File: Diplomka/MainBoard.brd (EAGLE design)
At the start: 100 x 100 mm, 44 parts, among them K1 ARK550/2, Q1 AP2012P3C-P22, Q2 BC817-40LT1SMD, Q3 SS8050-G, Q4 SS8050-G, U1 ESP32-WROOM-32, U2 AMS1117-3.3

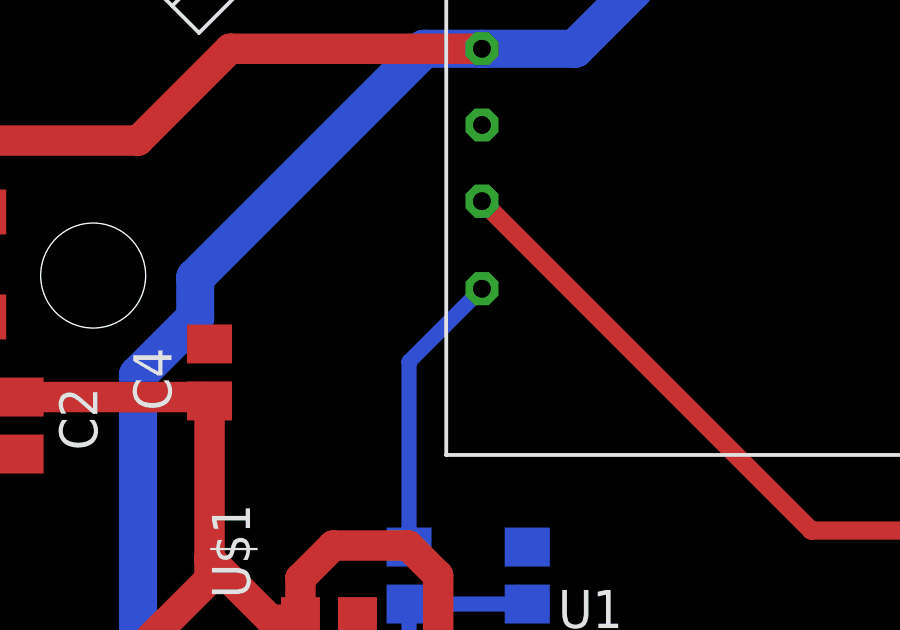
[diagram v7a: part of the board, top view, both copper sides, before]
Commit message: Opravena rozteč.
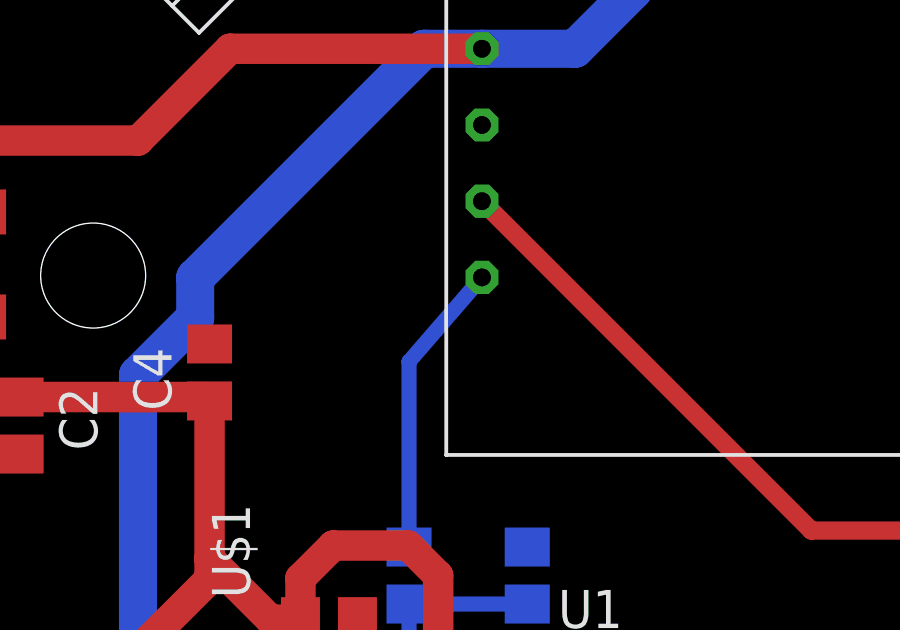
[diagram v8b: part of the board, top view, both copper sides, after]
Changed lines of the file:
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@@
 <via x="42.5" y="93.5" extent="1-16" drill="0.5" diameter="1.15" shape="octagon"/>
 <contactref element="JUM1" pad="6"/>
+<wire x1="64.97" y1="66.48" x2="85" y2="78.85" width="0" layer="19" extent="1-1"/>
+<wire x1="58.5" y1="55.26" x2="64.97" y2="66.48" width="0" layer="19" extent="1-1"/>
+<wire x1="50.835" y1="49.595" x2="58.5" y2="55.26" width="0" layer="19" extent="1-1"/>
+<wire x1="50.835" y1="48.6775" x2="50.835" y2="49.595" width="0" layer="19" extent="1-1"/>
+<wire x1="50.835" y1="47.76" x2="50.835" y2="48.6775" width="0" layer="19" extent="1-1"/>
+<wire x1="49.9175" y1="49.595" x2="50.835" y2="49.595" width="0" layer="19" extent="1-1"/>
+<wire x1="49" y1="49.595" x2="49.9175" y2="49.595" width="0" layer="19" extent="1-1"/>
+<wire x1="49" y1="48.6775" x2="49" y2="49.595" width="0" layer="19" extent="1-1"/>
+<wire x1="50.835" y1="46.8425" x2="50.835" y2="47.76" width="0" layer="19" extent="1-1"/>
+<wire x1="50.835" y1="45.925" x2="50.835" y2="46.8425" width="0" layer="19" extent="1-1"/>
+<wire x1="49" y1="47.76" x2="49" y2="48.6775" width="0" layer="19" extent="1-1"/>
+<wire x1="48.0825" y1="49.595" x2="49" y2="49.595" width="0" layer="19" extent="1-1"/>
+<wire x1="47.165" y1="49.595" x2="48.0825" y2="49.595" width="0" layer="19" extent="1-1"/>
+<wire x1="47.165" y1="48.6775" x2="47.165" y2="49.595" width="0" layer="19" extent="1-1"/>
+<wire x1="49.9175" y1="47.76" x2="50.835" y2="47.76" width="0" layer="19" extent="1-1"/>
+<wire x1="49" y1="46.8425" x2="49" y2="47.76" width="0" layer="19" extent="1-1"/>
+<wire x1="49" y1="45.925" x2="49" y2="46.8425" width="0" layer="19" extent="1-1"/>
+<wire x1="49.9175" y1="45.925" x2="50.835" y2="45.925" width="0" layer="19" extent="1-1"/>
+<wire x1="47.165" y1="47.76" x2="47.165" y2="48.6775" width="0" layer="19" extent="1-1"/>
+<wire x1="48.0825" y1="47.76" x2="49" y2="47.76" width="0" layer="19" extent="1-1"/>
+<wire x1="47.165" y1="46.8425" x2="47.165" y2="47.76" width="0" layer="19" extent="1-1"/>
+<wire x1="47.165" y1="45.925" x2="47.165" y2="46.8425" width="0" layer="19" extent="1-1"/>
+<wire x1="48.0825" y1="45.925" x2="49" y2="45.925" width="0" layer="19" extent="1-1"/>
+<wire x1="41.5" y1="55.26" x2="47.165" y2="49.595" width="0" layer="19" extent="1-1"/>
+<wire x1="44.285" y1="37.75" x2="47.165" y2="45.925" width="0" layer="19" extent="1-1"/>
+<wire x1="50.44" y1="30.68" x2="44.285" y2="37.75" width="0" layer="19" extent="1-1"/>
+<wire x1="39.47" y1="65.95" x2="41.5" y2="55.26" width="0" layer="19" extent="1-16"/>
+<wire x1="61.17" y1="33.58" x2="50.44" y2="30.68" width="0" layer="19" extent="1-1"/>
+<wire x1="35.03" y1="46.2" x2="41.5" y2="55.26" width="0" layer="19" extent="1-1"/>
+<wire x1="27" y1="43" x2="35.03" y2="46.2" width="0" layer="19" extent="1-1"/>
+<wire x1="26.495" y1="48.26" x2="27" y2="43" width="0" layer="19" extent="1-1"/>
+<wire x1="32.04" y1="37.97" x2="27" y2="43" width="0" layer="19" extent="1-1"/>
+<wire x1="29.5" y1="56.08" x2="26.495" y2="48.26" width="0" layer="19" extent="1-1"/>
+<wire x1="28.88" y1="72.72" x2="39.47" y2="65.95" width="0" layer="19" extent="1-16"/>
+<wire x1="22.6" y1="69.05" x2="28.88" y2="72.72" width="0" layer="19" extent="1-1"/>
+<wire x1="21.45" y1="73.62" x2="22.6" y2="69.05" width="0" layer="19" extent="1-1"/>
+<wire x1="21.45" y1="77.12" x2="21.45" y2="73.62" width="0" layer="19" extent="1-1"/>
+<wire x1="16.465" y1="69.34" x2="22.6" y2="69.05" width="0" layer="19" extent="1-1"/>
+<wire x1="37.96" y1="80.02" x2="28.88" y2="72.72" width="0" layer="19" extent="1-1"/>
+<wire x1="31.32825" y1="85.828246875" x2="37.96" y2="80.02" width="0" layer="19" extent="16-16"/>
+<wire x1="29.99" y1="89.04" x2="31.32825" y2="85.828246875" width="0" layer="19" extent="16-16"/>
+<wire x1="35" y1="89.2" x2="31.32825" y2="85.828246875" width="0" layer="19" extent="16-16"/>
+<wire x1="36.95" y1="94.5" x2="35" y2="89.2" width="0" layer="19" extent="16-16"/>
+<wire x1="41.05" y1="91" x2="36.95" y2="94.5" width="0" layer="19" extent="16-16"/>
+<wire x1="41.05" y1="88.5" x2="41.05" y2="91" width="0" layer="19" extent="16-16"/>
+<wire x1="42.5" y1="93.5" x2="41.05" y2="91" width="0" layer="19" extent="16-16"/>
+<wire x1="74.544" y1="37.828" x2="61.17" y2="33.58" width="0" layer="19" extent="1-1"/>
+<wire x1="74.4" y1="54.23" x2="64.97" y2="66.48" width="0" layer="19" extent="1-1"/>
+<wire x1="61.47" y1="16.95" x2="61.17" y2="33.58" width="0" layer="19" extent="1-1"/>
+<wire x1="31" y1="16.08" x2="32.04" y2="37.97" width="0" layer="19" extent="1-1"/>
 </signal>
 <signal name="3V3">
@@
 <contactref element="U$2" pad="AO"/>
 <contactref element="R4" pad="2"/>
-<wire x1="37.96" y1="74.56" x2="35.53" y2="72.13" width="0.508" layer="16"/>
+<wire x1="37.96" y1="74.94" x2="35.53" y2="72.13" width="0.508" layer="16"/>
 <wire x1="35.53" y1="72.13" x2="35.53" y2="65.95" width="0.508" layer="16"/>
 </signal>
